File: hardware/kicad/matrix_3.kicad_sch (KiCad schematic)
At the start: 135 parts, among them U7 IS31FL3741A

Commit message: Update KiCAD files
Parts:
- removed R108, R109: 4.7k, Resistor_SMD:R_0402_1005Metric, symbol Device:R_Small_US

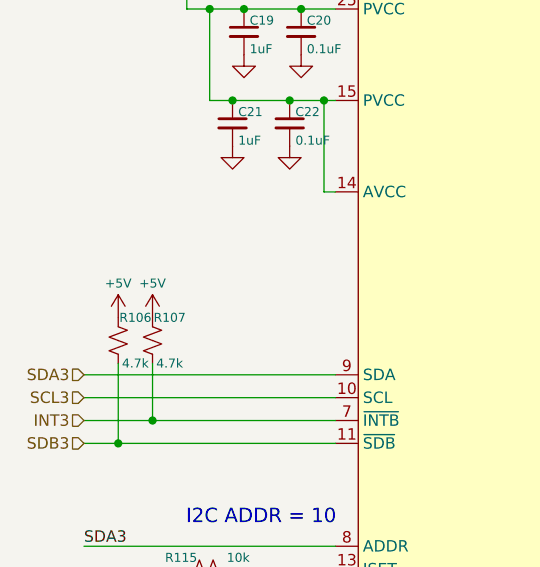
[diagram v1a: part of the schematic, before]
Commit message: Update KiCAD files
correct files this time :)
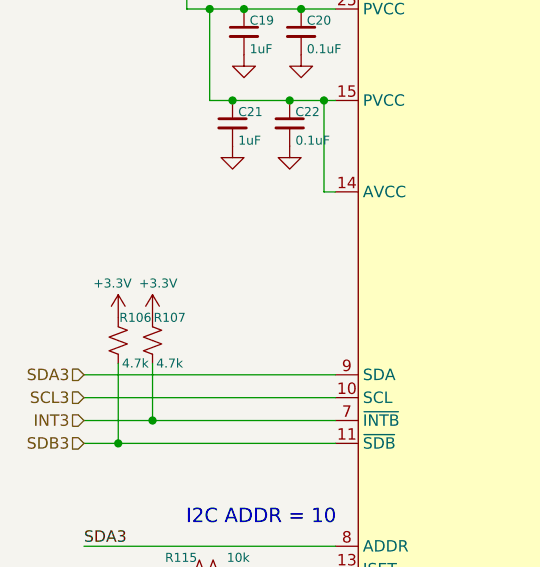
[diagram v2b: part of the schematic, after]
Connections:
- net +5V: no longer R106.1, R107.1
- new net +3.3V: R106.1, R107.1
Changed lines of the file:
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@@
 	)
 	(symbol
-		(lib_id "power:+5V")
-		(at 40.64 72.39 0)
-		(unit 1)
-		(exclude_from_sim no)
-		(in_bom yes)
-		(on_board yes)
-		(dnp no)
-		(property "Reference" "#PWR081"
-			(at 40.64 76.2 0)
-			(effects
-				(font
-					(size 1.27 1.27)
-				)
-				(hide yes)
-			)
-		)
-		(property "Value" "+5V"
-			(at 40.64 68.58 0)
-			(effects
-				(font
-					(size 1 1)
-				)
-			)
-		)
-		(property "Footprint" ""
-			(at 40.64 72.39 0)
-			(effects
-				(font
-					(size 1.27 1.27)
-				)
-				(hide yes)
-			)
-		)
-		(property "Datasheet" ""
-			(at 40.64 72.39 0)
-			(effects
-				(font
-					(size 1.27 1.27)
-				)
-				(hide yes)
-			)
-		)
-		(property "Description" "Power symbol creates a global label with name \"+5V\""
-			(at 40.64 72.39 0)
-			(effects
-				(font
-					(size 1.27 1.27)
-				)
-				(hide yes)
-			)
-		)
-		(pin "1"
-		)
-		(instances
-			(project "v0"
-				(path "/911505fc-874d-4338-908e-12054bdd5112/8dd6618c-1a80-4fae-a98a-23e19309c792"
-					(reference "#PWR081")
-					(unit 1)
-				)
-			)
-		)
-	)
-	(symbol
 		(lib_id "Device:LED_RABG")
 		(at 177.8 54.61 0)
@@
 	)
 	(symbol
+		(lib_id "power:+3.3V")
+		(at 40.64 72.39 0)
+		(unit 1)
+		(exclude_from_sim no)
+		(in_bom yes)
+		(on_board yes)
+		(dnp no)
+		(property "Reference" "#PWR059"
+			(at 40.64 76.2 0)
+			(effects
+				(font
+					(size 1.27 1.27)
+				)
+				(hide yes)
+			)
+		)
+		(property "Value" "+3.3V"
+			(at 41.275 68.58 0)
+			(effects
+				(font
+					(size 1 1)
+				)
+			)
+		)
+		(property "Footprint" ""
+			(at 40.64 72.39 0)
+			(effects
+				(font
+					(size 1.27 1.27)
+				)
+				(hide yes)
+			)
+		)
+		(property "Datasheet" ""
+			(at 40.64 72.39 0)
+			(effects
+				(font
+					(size 1.27 1.27)
+				)
+				(hide yes)
+			)
+		)
+		(property "Description" "Power symbol creates a global label with name \"+3.3V\""
+			(at 40.64 72.39 0)
+			(effects
+				(font
+					(size 1.27 1.27)
+				)
+				(hide yes)
+			)
+		)
+		(pin "1"
+		)
+		(instances
+			(project "traffic_paradise"
+				(path "/911505fc-874d-4338-908e-12054bdd5112/8dd6618c-1a80-4fae-a98a-23e19309c792"
+					(reference "#PWR059")
+					(unit 1)
+				)
+			)
+		)
+	)
+	(symbol
 		(lib_id "Device:C_Small")
 		(at 57.15 40.64 0)
@@
 	)
 	(symbol
+		(lib_id "power:+3.3V")
+		(at 36.83 72.39 0)
+		(unit 1)
+		(exclude_from_sim no)
+		(in_bom yes)
+		(on_board yes)
+		(dnp no)
+		(property "Reference" "#PWR058"
+			(at 36.83 76.2 0)
+			(effects
+				(font
+					(size 1.27 1.27)
+				)
+				(hide yes)
+			)
+		)
+		(property "Value" "+3.3V"
+			(at 36.195 68.58 0)
+			(effects
+				(font
+					(size 1 1)
+				)
+			)
+		)
+		(property "Footprint" ""
+			(at 36.83 72.39 0)
+			(effects
+				(font
+					(size 1.27 1.27)
+				)
+				(hide yes)
+			)
+		)
+		(property "Datasheet" ""
+			(at 36.83 72.39 0)
+			(effects
+				(font
+					(size 1.27 1.27)
+				)
+				(hide yes)
+			)
+		)
+		(property "Description" "Power symbol creates a global label with name \"+3.3V\""
+			(at 36.83 72.39 0)
+			(effects
+				(font
+					(size 1.27 1.27)
+				)
+				(hide yes)
+			)
+		)
+		(pin "1"
+		)
+		(instances
+			(project "traffic_paradise"
+				(path "/911505fc-874d-4338-908e-12054bdd5112/8dd6618c-1a80-4fae-a98a-23e19309c792"
+					(reference "#PWR058")
+					(unit 1)
+				)
+			)
+		)
+	)
+	(symbol
 		(lib_id "Device:R_Small_US")
 		(at 137.16 93.98 90)
@@
 					(unit 1)
 				)
-			)
-		)
-	)
-	(symbol
-		(lib_id "power:+5V")
-		(at 36.83 72.39 0)
-		(unit 1)
-		(exclude_from_sim no)
-		(in_bom yes)
-		(on_board yes)
-		(dnp no)
-		(property "Reference" "#PWR080"
-			(at 36.83 76.2 0)
-			(effects
-				(font
-					(size 1.27 1.27)
-				)
-				(hide yes)
-			)
-		)
-		(property "Value" "+5V"
-			(at 36.83 68.58 0)
-			(effects
-				(font
-					(size 1 1)
-				)
-			)
-		)
-		(property "Footprint" ""
-			(at 36.83 72.39 0)
-			(effects
-				(font
-					(size 1.27 1.27)
-				)
-				(hide yes)
-			)
-		)
-		(property "Datasheet" ""
-			(at 36.83 72.39 0)
-			(effects
-				(font
-					(size 1.27 1.27)
-				)
-				(hide yes)
-			)
-		)
-		(property "Description" "Power symbol creates a global label with name \"+5V\""
-			(at 36.83 72.39 0)
-			(effects
-				(font
-					(size 1.27 1.27)
-				)
-				(hide yes)
-			)
-		)
-		(pin "1"
-		)
-		(instances
-			(project "v0"
-				(path "/911505fc-874d-4338-908e-12054bdd5112/8dd6618c-1a80-4fae-a98a-23e19309c792"
-					(reference "#PWR080")
-					(unit 1)
-				)

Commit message: Added LED key, update LED, some other changes
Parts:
- added LED325, LED326, LED327, LED328: LED_ARGB, map_lbr:LED_RGB_0606, symbol Device:LED_RABG
- added R109: 51, Resistor_SMD:R_0402_1005Metric, symbol Device:R_Small_US
- added R145, R146: 20, Resistor_SMD:R_0402_1005Metric, symbol Device:R_Small_US
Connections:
- net COL0: now also LED325.2 (A)
- net COL1: now also LED326.2 (A)
- net COL2: now also LED327.2 (A)
- net COL3: now also LED328.2 (A)
- net IND_B: now reaches U7.1 (CS34)
- net IND_B: now also R146.1
- net IND_G: now reaches U7.2 (CS35)
- net IND_G: now also R145.1
- net IND_R: now reaches U7.3 (CS36)
- net IND_R: now also R109.1
- new net: LED325.3 (BK), LED326.3 (BK), LED327.3 (BK), LED328.3 (BK), R146.2
- new net: LED325.1 (RK), LED326.1 (RK), LED327.1 (RK), LED328.1 (RK), R109.2
- new net: LED325.4 (GK), LED326.4 (GK), LED327.4 (GK), LED328.4 (GK), R145.2

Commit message: Modified silkscreen, generated production files
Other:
- note added: "OTA"
- note added: "Traffic Key"
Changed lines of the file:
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@@
+		)
+	)
+	(rectangle
+		(start 144.78 233.68)
+		(end 182.88 255.27)
+		(stroke
+			(width 0)
+			(type dash)
+		)
+		(fill
+			(type none)
+		)
+	)
+	(rectangle
+		(start 184.15 233.68)
+		(end 195.58 255.27)
+		(stroke
+			(width 0)
+			(type dash)
+		)
+		(fill
+			(type none)
+		)
+	)
+	(text "OTA"
+		(exclude_from_sim no)
+		(at 193.675 257.175 0)
+		(effects
+			(font
+				(size 1.27 1.27)
+			)
 		)
 	)
@@
 			)
 		)
+	)
+	(text "Traffic Key"
+		(exclude_from_sim no)
+		(at 149.86 257.175 0)
+		(effects
+			(font
+				(size 1.27 1.27)
+			)
+		)

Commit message: add leds to 126 segment
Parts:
- added LED331, LED332, LED333: LED_ARGB, map_lbr:LED_RGB_0606, symbol Device:LED_RABG
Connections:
- net COL0: now also LED331.2 (A)
- net COL1: now also LED332.2 (A)
- net COL2: now also LED333.2 (A)
- net at LED329.1 (RK), LED330.1 (RK), R134.2: now also LED331.1 (RK), LED332.1 (RK), LED333.1 (RK)
- net at LED329.3 (BK), LED330.3 (BK), R136.2: now also LED331.3 (BK), LED332.3 (BK), LED333.3 (BK)
- net at LED329.4 (GK), LED330.4 (GK), R135.2: now also LED331.4 (GK), LED332.4 (GK), LED333.4 (GK)

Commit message: add and route matrix 4
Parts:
- removed LED314, LED318, LED319, LED320, LED321, LED322, LED323, LED324, LED325, LED326, LED327, LED328, LED329, LED330, LED331, LED332, LED333: LED_ARGB, map_lbr:LED_RGB_0606, symbol Device:LED_RABG
- added LED167, LED168, LED169, LED170, LED171, LED380, LED381, LED382, LED383, LED384, LED385, LED386, LED387: LED_ARGB, map_lbr:LED_RGB_0606, symbol Device:LED_RABG
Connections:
- net COL0: now also LED167.2 (A), LED383.2 (A); no longer LED307.2 (A)
- net COL1: now also LED168.2 (A), LED384.2 (A); no longer LED308.2 (A)
- net COL2: now also LED307.2 (A), LED169.2 (A), LED385.2 (A); no longer LED309.2 (A)
- net COL3: now also LED308.2 (A), LED170.2 (A), LED386.2 (A); no longer LED310.2 (A)
- net COL4: now also LED309.2 (A), LED171.2 (A), LED387.2 (A); no longer LED311.2 (A)
- net COL5: now also LED310.2 (A), LED311.2 (A); no longer LED312.2 (A)
- net COL6: now also LED312.2 (A), LED380.2 (A); no longer LED313.2 (A)
- net COL7: now also LED313.2 (A), LED381.2 (A)
- net COL8: now also LED382.2 (A)
- net at R134.2: now also LED383.1 (RK), LED384.1 (RK), LED385.1 (RK), LED386.1 (RK), LED387.1 (RK)
- net at R136.2: now also LED383.3 (BK), LED384.3 (BK), LED385.3 (BK), LED386.3 (BK), LED387.3 (BK)
- net at R135.2: now also LED383.4 (GK), LED384.4 (GK), LED385.4 (GK), LED386.4 (GK), LED387.4 (GK)
- net at LED316.1 (RK), LED317.1 (RK), R131.2: now also LED307.1 (RK), LED308.1 (RK), LED309.1 (RK), LED310.1 (RK), LED380.1 (RK), LED381.1 (RK), LED382.1 (RK)
- net at LED316.3 (BK), LED317.3 (BK), R133.2: now also LED307.3 (BK), LED308.3 (BK), LED309.3 (BK), LED310.3 (BK), LED380.3 (BK), LED381.3 (BK), LED382.3 (BK)
- net at LED316.4 (GK), LED317.4 (GK), R132.2: now also LED307.4 (GK), LED308.4 (GK), LED309.4 (GK), LED310.4 (GK), LED380.4 (GK), LED381.4 (GK), LED382.4 (GK)
- net at LED311.1 (RK), LED312.1 (RK), LED313.1 (RK)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: now also LED167.1 (RK), LED168.1 (RK), LED169.1 (RK), LED170.1 (RK), LED171.1 (RK); no longer LED307.1 (RK), LED308.1 (RK), LED309.1 (RK), LED310.1 (RK)
- net at LED311.3 (BK), LED312.3 (BK), LED313.3 (BK)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: now also LED167.3 (BK), LED168.3 (BK), LED169.3 (BK), LED170.3 (BK), LED171.3 (BK); no longer LED307.3 (BK), LED308.3 (BK), LED309.3 (BK), LED310.3 (BK)
- net at LED311.4 (GK), LED312.4 (GK), LED313.4 (GK)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: now also LED167.4 (GK), LED168.4 (GK), LED169.4 (GK), LED170.4 (GK), LED171.4 (GK); no longer LED307.4 (GK), LED308.4 (GK), LED309.4 (GK), LED310.4 (GK)
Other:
- note removed: "OTA"
- note removed: "Traffic Key"

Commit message: esp32c3 upgrade, route usb, fix errors
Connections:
- net GND: now also U7.8 (ADDR)
- net SDA3: no longer U7.8 (ADDR)
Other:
- note added: "I2C ADDR = 00"
- note added: "I2C2"
- note removed: "I2C ADDR = 10"
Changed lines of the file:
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@@
 	)
 	(junction
+		(at 40.64 100.33)
+		(diameter 0)
+		(color 0 0 0 0)
+	)
+	(junction
 		(at 234.95 189.23)
 		(diameter 0)
@@
 	(wire
 		(pts
-			(xy 33.02 97.79) (xy 60.96 97.79)
-		)
-		(stroke
-			(width 0)
-			(type default)
-		)
-	)
-	(wire
-		(pts
 			(xy 184.15 106.68) (xy 185.42 106.68)
 		)
@@
 	(wire
 		(pts
+			(xy 40.64 97.79) (xy 40.64 100.33)
+		)
+		(stroke
+			(width 0)
+			(type default)
+		)
+	)
+	(wire
+		(pts
 			(xy 182.88 54.61) (xy 182.88 73.66)
 		)
@@
 	(wire
 		(pts
+			(xy 60.96 97.79) (xy 40.64 97.79)
+		)
+		(stroke
+			(width 0)
+			(type default)
+		)
+	)
+	(wire
+		(pts
 			(xy 196.85 137.16) (xy 196.85 135.89)
 		)
@@
 		)
 	)
-	(text "I2C ADDR = 10\n"
+	(text "I2C2"
+		(exclude_from_sim no)
+		(at 52.07 77.216 0)
+		(effects
+			(font
+				(size 1.27 1.27)
+			)
+		)
+	)
+	(text "I2C ADDR = 00"
 		(exclude_from_sim no)
 		(at 52.705 94.615 0)
@@
 		)
 	)
-	(label "SDA3"
-		(at 33.02 97.79 0)
-		(fields_autoplaced yes)
-		(effects
-			(font
-				(size 1.27 1.27)
-			)
-			(justify left bottom)
-		)
-	)
